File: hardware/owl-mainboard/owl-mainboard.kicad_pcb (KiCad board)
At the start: 4 copper layers, 61.8 x 79.8 mm, 107 parts, among them J101 Battery +, -, J201 USB-C, J202 EXP: GND, 3V3, A, B, J301 AMOLED FPC, J302 LRA, J303 DOCK: GND, VBUS, DET, GND, SW201 Ear left, SW202 Ear right, SW203 Beak, U101 BQ24073RGTR, U102 MAX17048G+T10, U103 TPS63802DLAR, U104 TPS22917DBVR, U201 ESP32-S3-WROOM-1-N16R8, U202 USBLC6-2SC6, U301 DRV2605LDGSR, U302 TMAG5273A2QDBVR, U303 LIS2DW12TR, U304 OPT3001DNPR, Y201 32.768kHz 12.5pF

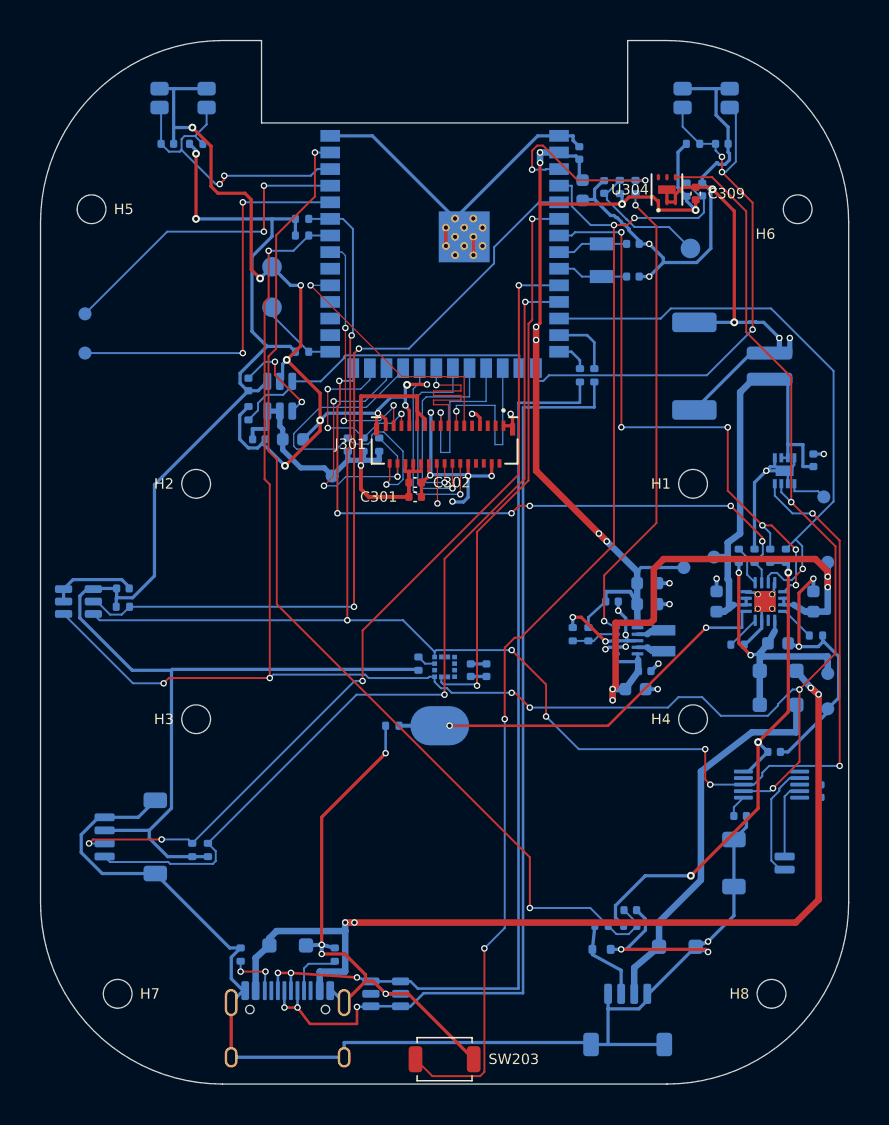
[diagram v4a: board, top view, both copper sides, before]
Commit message: feat(hardware): pour the outer GND, stitch the edge and finish the routes Freerouting left
hw_route.py groups:
- outer_pours: GND on F.Cu and B.Cu over the whole board (0.2 mm
  clearance, thermal reliefs), drawn after the Freerouting import.
- stitching: 68 GND vias about every 3 mm on a line 0.75 mm inside
  the edge (R5) and along the antenna notch's lower edge under the
  module; spots against other copper, any pad, a mounting hole or under
  J201 are left out.
- local_power: the fine-pitch power pins Freerouting could not reach
  with the Power class's 0.2 mm clearance. U303: +3V3 pad 2 to R309 and
  across under the LGA to pads 9, 10 and C307, plus a GND via for its
  GND pads (a pour island). U301: GND pin 8 to C304 and a via, +3V3 pin
  10 to C304 and a via with an F.Cu link to the +3V3 run over the
  package, pins 6 and 5 joined under the package, GND pin 4 to a via.
  C202: its GND pad to module pin 1.
- vbus_usb: the right-side F.Cu run moves from x 28.6 to 29.4, east of
  C304, so U301's and C304's vias fit.
- j301_fanout: LCD_RST on to module pin 32 by hand (B.Cu at y 7.3,
  F.Cu at x -10.1, B.Cu round LCD_TE's stub and via).

DRU: J201's shell tabs join the pours solid and C202's GND pad keeps
off the B.Cu pour (both had one thermal spoke; C202 has its own track).

Routed copper changed by hand: I2C_SDA's leg from U301 to the right
edge deleted (it blocked the stitching and U301's +3V3), Freerouting's
GND F.Cu chain west of the module and two GND B.Cu stubs deleted (the
pours carry GND there), and three hole-clearance spots fixed by moving
two TP_INT bends 0.06 mm, a TP_SCL via 0.04 mm and a TP_RST via
0.08 mm.

DRC: no violation besides the silkscreen ones; 4 unconnected left
(+3V3 twice, I2C_SDA to U304 and U102), routed next.
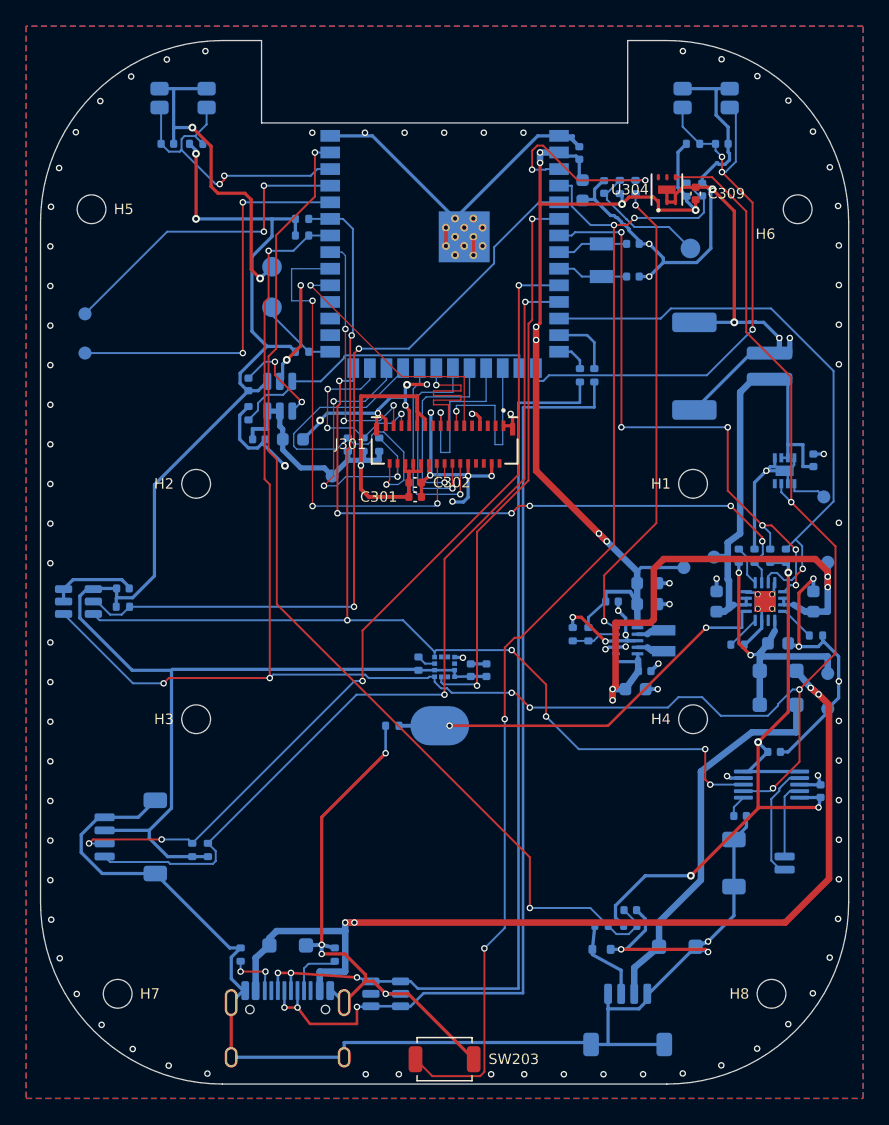
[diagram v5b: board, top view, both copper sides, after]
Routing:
- net I2C_SDA: track 124.9 -> 92.2 mm, vias 8 -> 6
- net LCD_RST: track 3.06 -> 35.4 mm, vias 1 -> 3
- net +3V3: track 228.3 -> 244.0 mm, vias 13 -> 14
- net GND: track 411.4 -> 404.4 mm, vias 45 -> 116
- added copper zone on B.Cu, net GND
- added copper zone on F.Cu, net GND

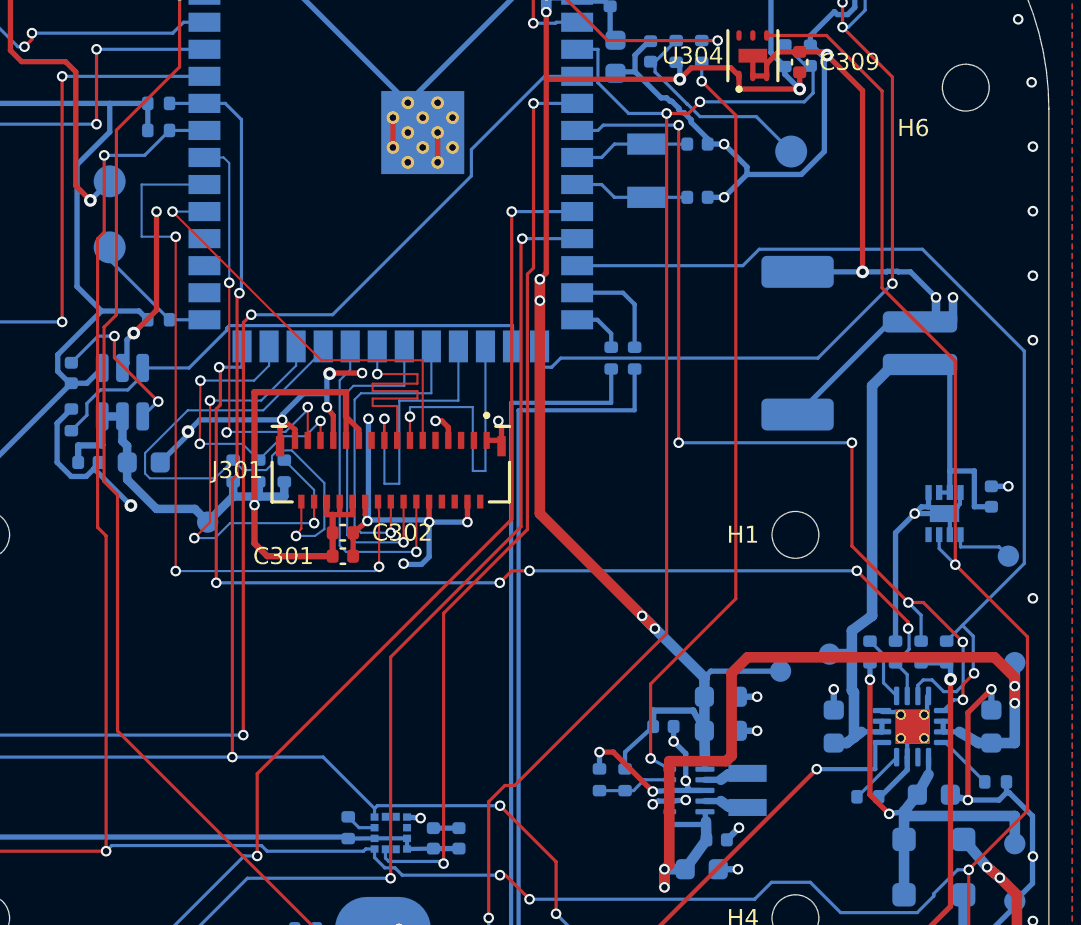
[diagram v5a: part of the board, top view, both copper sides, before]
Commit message: feat(hardware): join the two +3V3 islands Freerouting left to the TPS63802 output
Freerouting's +3V3 ended in three groups. The new late_links group in
hw_route.py joins them by hand:
- the west group (U104 pin 1, C110, R206, R207, R210, R211, R304 to
  R306, R309, U302, U303, C306 to C308, J202): a via beside R306's
  +3V3 pad, F.Cu east at y 27.5 over the module's left column (below
  DOCK_DET's F.Cu run) and a via into the In2 +3V3 pour under the
  module;
- the U301 group (U301, C304, C305, R105, R106, R308): F.Cu from its
  via at (26.28, 2.22) west at y 2.5 to a via beside TP104 on the
  TPS63802 output. vin_chg_taps' top via moves from y 2.2 to 1.8 so
  that run fits between it and the VSYS F.Cu run at y 3.25.

DRC: no violation besides the silkscreen ones; 2 unconnected left
(I2C_SDA to U304 and U102).
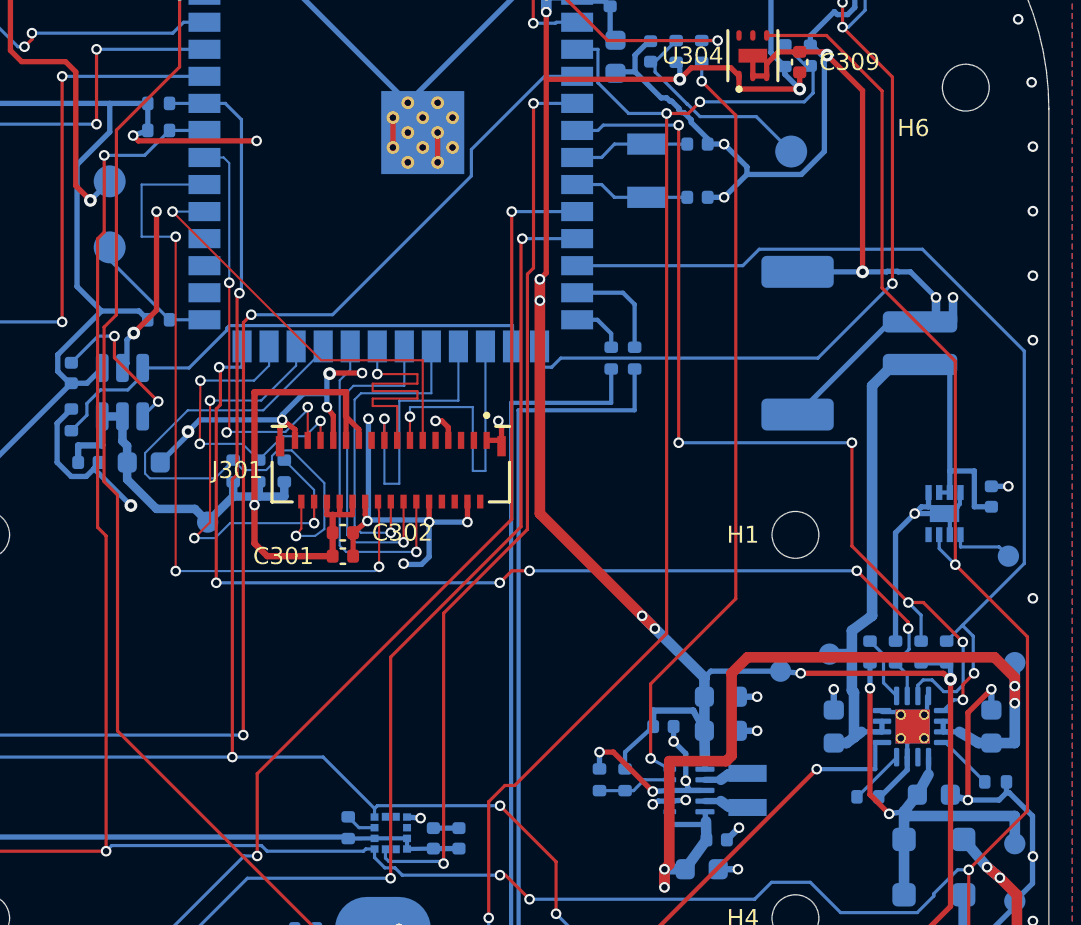
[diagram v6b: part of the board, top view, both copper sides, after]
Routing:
- net +3V3: track 244.0 -> 258.8 mm, vias 14 -> 17

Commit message: feat(hardware): route the last two I2C_SDA links by hand
Freerouting left U304 pin 6 and U102 pin 8 off the bus. Both links are
hand copper in hw_route.py late_links:

- U304 pin 6 runs F.Cu west above ESP_EN's run and over the +3V3 vias at
  x 7.3, then B.Cu under the module to the SDA run from pin 35.
- U102 pin 8 runs F.Cu north round CHG_PGOOD's via, south at x 20.5, hops
  under the VSYS and +3V3 F.Cu runs on B.Cu and joins the bus via at
  (19.929, -11.292) on the U301 side.

Three Freerouting GND tracks under the module that crossed the first path
are deleted; the B.Cu pour joins those module pads. DRC: 0 unconnected,
0 parity, only the Task 8 silkscreen warnings left.
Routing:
- net I2C_SDA: track 92.2 -> 157.2 mm, vias 6 -> 10
- net GND: track 404.4 -> 385.9 mm

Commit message: feat(hardware): add GND return vias beside the J201-side USB vias
The USB pair changes reference from In2 to In1 at the vias next to J201,
and the nearest GND through-connection was the shell tab 3.6 mm away
(Step 1 review M6). One GND via now sits above the two D+ vias and one
below the two D- vias; at the U202 end the shell tab is beside the vias
already. DRC unchanged: 0 unconnected, 0 parity, silkscreen warnings only.
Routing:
- net GND: vias 116 -> 118
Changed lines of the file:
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@@
 	)
 	(via
+		(at 87.75 127.65)
+		(size 0.5)
+		(drill 0.3)
+		(layers "F.Cu" "B.Cu")
+		(locked yes)
+		(net "GND")
+	)
+	(via
 		(at 73.77 132.37)
 		(size 0.5)
@@
 	)
 	(via
+		(at 88.25 131.949999)
+		(size 0.5)
+		(drill 0.3)
+		(layers "F.Cu" "B.Cu")
+		(locked yes)
+		(net "GND")
+	)
+	(via
 		(at 94.9 85.6)
 		(size 0.5)
@@
 	)
 	(segment
-		(start 87.25 128.4)
-		(end 88.25 128.4)
+		(start 88.25 128.4)
+		(end 93.3 128.75)
 		(width 0.2)
 		(locked yes)
@@
 	)
 	(segment
-		(start 88.25 128.4)
-		(end 93.3 128.75)
+		(start 87.25 128.4)
+		(end 88.25 128.4)
 		(width 0.2)
 		(locked yes)
@@
 	)
 	(via
-		(at 93.3 128.75)
+		(at 88.25 128.4)
 		(size 0.5)
 		(drill 0.3)
@@
 	)
 	(via
-		(at 87.25 128.4)
+		(at 93.3 128.75)
 		(size 0.5)
 		(drill 0.3)
@@
 	)
 	(via
-		(at 88.25 128.4)
+		(at 87.25 128.4)
 		(size 0.5)
 		(drill 0.3)
@@
 	)
 	(segment
-		(start 87.25 129.755)
-		(end 87.25 128.4)
-		(width 0.2)
-		(locked yes)
-		(layer "B.Cu")
-		(net "USB_DP_CONN")
-	)
-	(segment
 		(start 97.4 129.05)
 		(end 97.95 129.6)
@@
 	)
 	(segment
-		(start 94.36 129.05)
-		(end 96.64 129.05)
+		(start 88.25 129.755)
+		(end 88.25 128.4)
 		(width 0.2)
 		(locked yes)
@@
 	)
 	(segment
-		(start 88.25 129.755)
-		(end 88.25 128.4)
+		(start 94.36 129.05)
+		(end 96.64 129.05)
 		(width 0.2)
 		(locked yes)
@@
 	)
 	(segment
-		(start 105.65 129.6)
-		(end 105.65 84.8)
+		(start 87.25 129.755)
+		(end 87.25 128.4)
 		(width 0.2)
 		(locked yes)
@@
 	)
 	(segment
-		(start 87.75 131.05)
-		(end 88.75 131.05)
+		(start 105.65 129.6)
+		(end 105.65 84.8)
 		(width 0.2)
 		(locked yes)
-		(layer "F.Cu")
-		(net "USB_DM_CONN")
+		(layer "B.Cu")
+		(net "USB_DP_CONN")
 	)
 	(segment
@@
 	)
 	(segment
+		(start 87.75 131.05)
+		(end 88.75 131.05)
+		(width 0.2)
+		(locked yes)
+		(layer "F.Cu")
+		(net "USB_DM_CONN")
+	)
+	(segment
 		(start 93.3 132.3)
 		(end 93.3 131)
@@
 	)
 	(via
-		(at 93.3 131)
+		(at 87.75 131.05)
 		(size 0.5)
 		(drill 0.3)
@@
 	)
 	(via
-		(at 87.75 131.05)
+		(at 93.3 131)
 		(size 0.5)
 		(drill 0.3)
@@
 	)
 	(segment
+		(start 88.75 129.755)
+		(end 88.75 131.05)
+		(width 0.2)
+		(locked yes)
+		(layer "B.Cu")
+		(net "USB_DM_CONN")
+	)
+	(segment
 		(start 97.4 130.949999)
 		(end 98.4 129.949999)
@@
 	)
 	(segment
-		(start 88.75 129.755)
-		(end 88.75 131.05)
-		(width 0.2)
-		(locked yes)
-		(layer "B.Cu")
-		(net "USB_DM_CONN")
-	)
-	(segment
 		(start 93.3 131)
 		(end 94.362 130.949999)
@@
 	)
 	(group "hw_route usb_fanout"
-		(members "067b724e-4d04-44ab-8184-95f1b632ebad" "21569469-0d18-44b6-9b45-a7bffaa6a939"
-			"2ce0cedf-c05f-4db1-a2af-4ba0865e6d6d" "38edbb4e-0767-45a6-b1b7-a0c4fd893913"
-			"40ae1243-a106-4e65-8d71-330d47dee5cd" "434a4c04-54c7-4acb-b45d-9acc5373ca1e"
-			"457327e4-0e72-4732-adb7-e77212e5757f" "4a2d6bcf-ad35-49d5-9810-850d027ee445"
-			"4e6ff9a8-7798-432d-a02b-ed42cce65178" "579474c7-6d0f-4aa0-9fa5-42a1c04d02d9"
-			"5dafad66-22c6-4934-b7d7-2ee2d835d02e" "60414c52-b40e-4bbb-a80d-b46fc9ece46a"
-			"90b3ac48-c20d-40f4-ba92-78e3563f9269" "9c19610e-6ad0-431c-b816-a9f5d2acfe48"
-			"c14ab183-c20c-4f12-879e-a79f57e9f98a" "e1c63799-0e3d-4773-a2a6-1cbd5464916c"
-			"f8d22fea-6bc6-4a3b-8f75-676d26d8220e" "f94c7ede-b571-4f59-927a-3e262213e577"
+		(members "054beec6-cbf7-4bf2-84a0-774d9da6e3d1" "0b81ea4e-170c-4ce2-8624-8fdad7984ddd"
+			"11342028-2d5e-4b95-b54b-3df0dc466259" "23cf29f9-951f-45bf-93de-932e08ccca9b"
+			"36b4e2f6-8f4a-4260-ba37-ce1e93d980d8" "551c06ac-0cb9-4d7e-acf9-3773fae902f7"
+			"5a9ddbdf-6d40-4137-90a1-74242ba83686" "64283048-a3ea-4f91-ad87-3fa405159f76"
+			"6cba4903-1f18-43ab-8ab1-0022e9299524" "8706cc13-fad2-4e41-ae46-7466d55e809c"
+			"942906ff-9414-423a-bbcd-958b529e9d6b" "9cc95267-756b-4156-b5f3-7bbc536e027c"
+			"a2b04bd4-576f-47da-a8c8-e22f1472dfb5" "ace56130-dc0c-4dc7-9e28-6ad1041be313"
+			"c49bd447-4e26-45fe-9787-c22d0a6f1944" "c763e254-8c69-44ab-ae23-486b82ff0055"
+			"cabbcb76-030e-4d4f-8566-cdbbe670b8c8" "d25c33ad-af79-4114-829a-bc2c317c9877"
+			"d524e060-fcda-4f00-b551-c6ec3ace14c0" "e13fff82-d99b-49cd-b947-ca4efdb9c082"
 		)
 	)
